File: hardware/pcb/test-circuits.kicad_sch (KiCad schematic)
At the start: 0 parts

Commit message: Update(hardware): Completed some schematics
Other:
- sheet Vibration LRA ports: added IN2, OUT+, OUT-; removed IN1
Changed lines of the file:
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@@
 		)
 		(pin "EN" input
+			(at 143.51 54.61 180)
+			(effects
+				(font
+					(size 1.27 1.27)
+				)
+				(justify left)
+			)
+		)
+		(pin "IN2" input
+			(at 143.51 60.96 180)
+			(effects
+				(font
+					(size 1.27 1.27)
+				)
+				(justify left)
+			)
+		)
+		(pin "OUT+" input
 			(at 165.1 54.61 0)
 			(effects
@@
 			)
 		)
-		(pin "IN1" input
+		(pin "OUT-" input
 			(at 165.1 60.96 0)
 			(effects

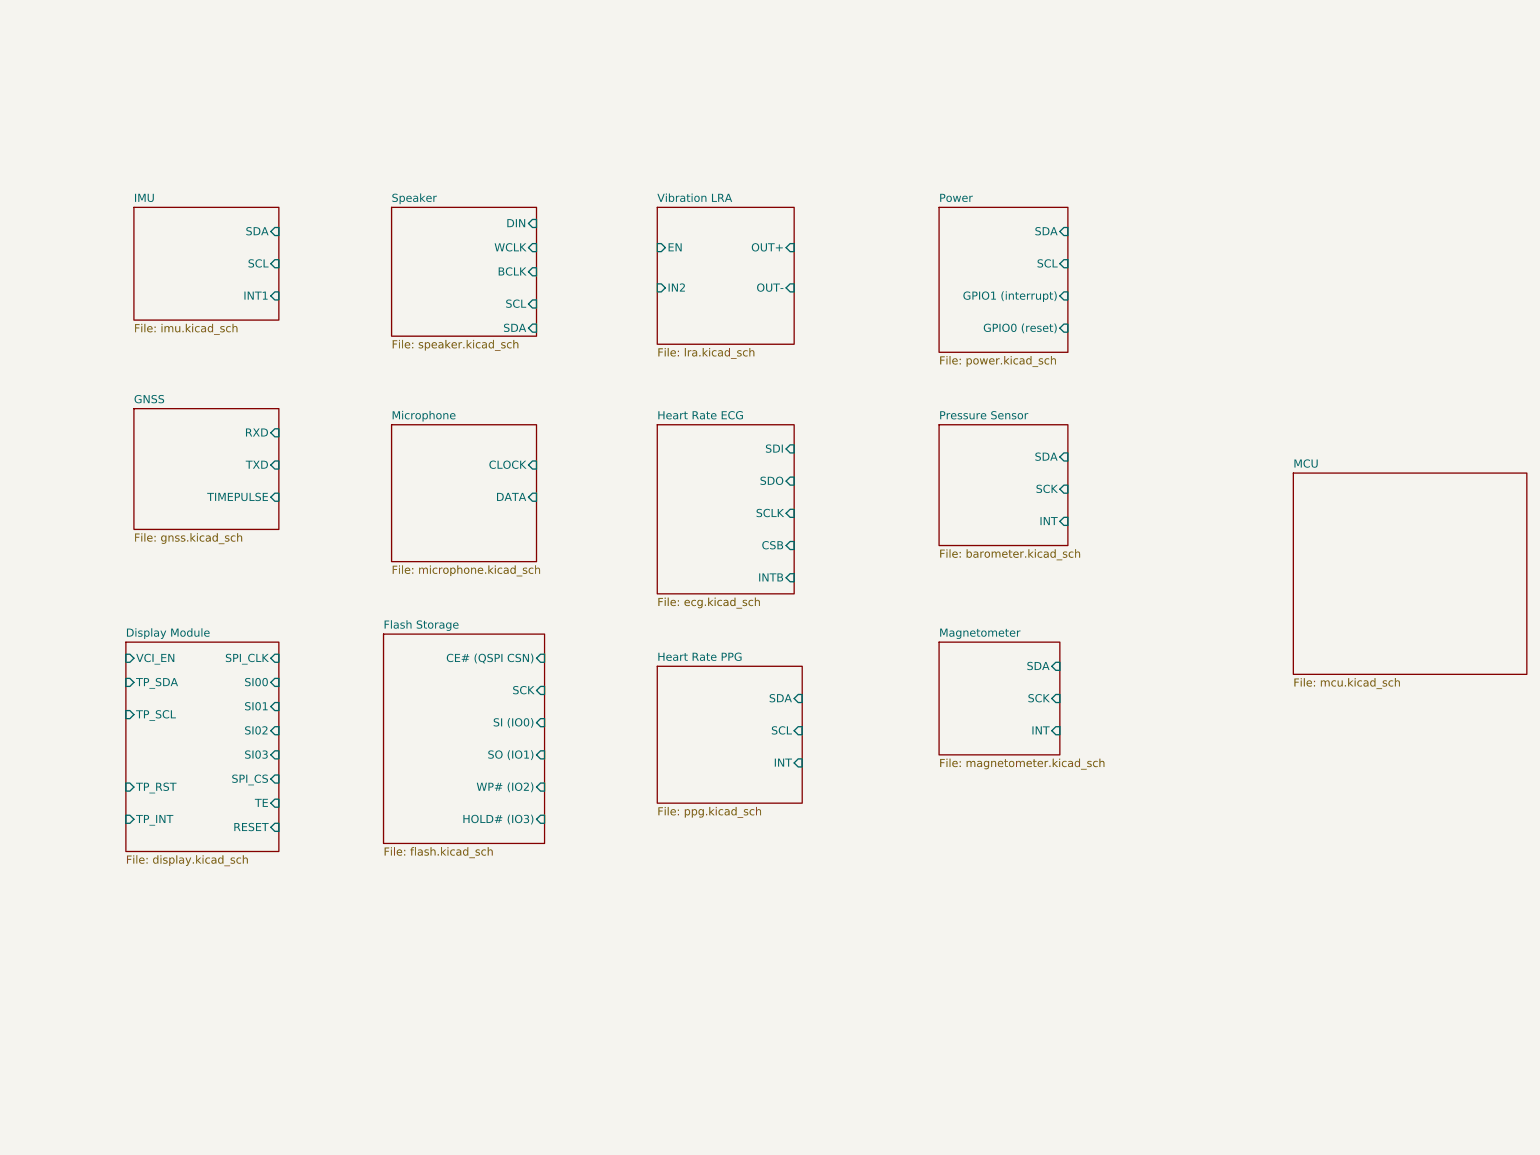
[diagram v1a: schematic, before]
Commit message: Changed GNDPWR to GND and changed GND to speciality GNDs
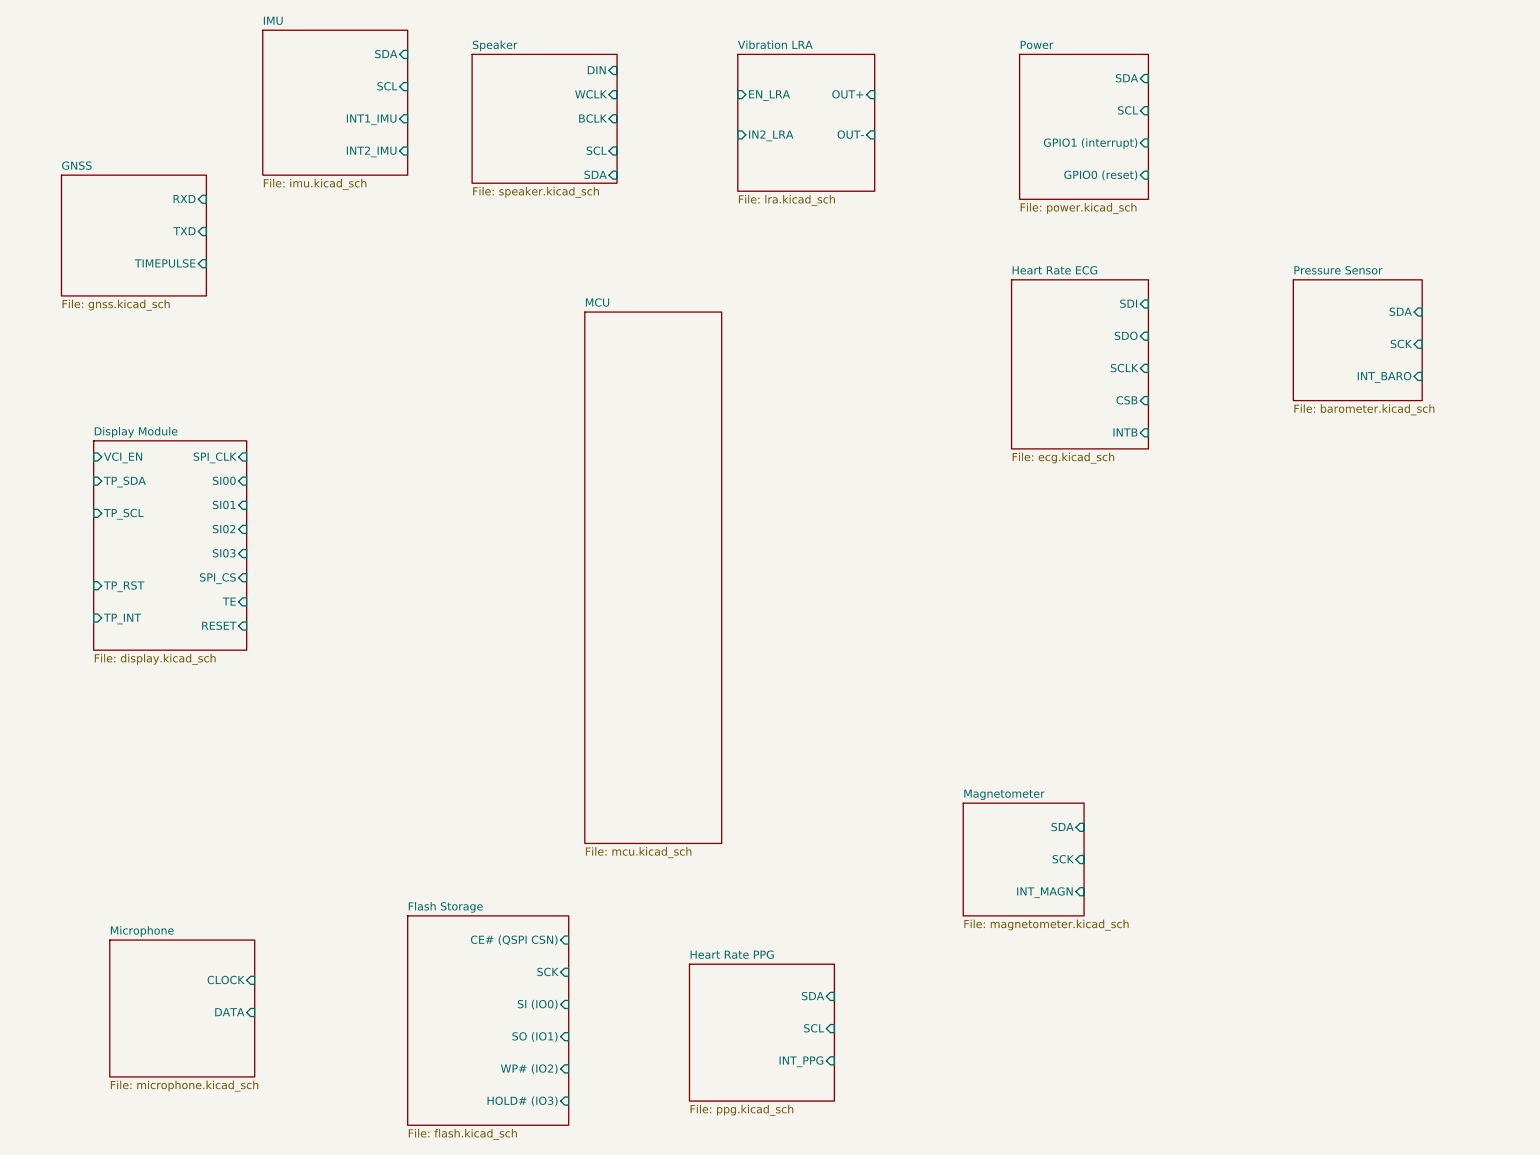
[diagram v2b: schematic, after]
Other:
- sheet Heart Rate PPG ports: added INT_PPG; removed INT
- sheet IMU ports: added INT1_IMU, INT2_IMU; removed INT1
- sheet Magnetometer ports: added INT_MAGN; removed INT
- sheet Pressure Sensor ports: added INT_BARO; removed INT
- sheet Vibration LRA ports: added EN_LRA, IN2_LRA; removed EN, IN2

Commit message: Added USB-C to UART connectivity for debugging and flashing
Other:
- added sheet Connector (connector.kicad_sch)
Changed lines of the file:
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@@
+	)
+	(sheet
+		(at 41.91 125.73)
+		(size 20.32 22.86)
+		(exclude_from_sim no)
+		(in_bom yes)
+		(on_board yes)
+		(dnp no)
+		(fields_autoplaced yes)
+		(stroke
+			(width 0.1524)
+			(type solid)
+		)
+		(fill
+			(color 0 0 0 0)
+		)
+		(property "Sheetname" "Connector"
+			(at 41.91 125.0184 0)
+			(show_name no)
+			(do_not_autoplace no)
+			(effects
+				(font
+					(size 1.27 1.27)
+				)
+				(justify left bottom)
+			)
+		)
+		(property "Sheetfile" "connector.kicad_sch"
+			(at 41.91 149.1746 0)
+			(show_name no)
+			(do_not_autoplace no)
+			(effects
+				(font
+					(size 1.27 1.27)
+				)
+				(justify left top)
+			)
+		)
+		(pin "DBG_UART_RXD" input
+			(at 62.23 129.54 0)
+			(effects
+				(font
+					(size 1.27 1.27)
+				)
+				(justify right)
+			)
+		)
+		(pin "DBG_UART_TXD" input
+			(at 62.23 134.62 0)
+			(effects
+				(font
+					(size 1.27 1.27)
+				)
+				(justify right)
+			)
+		)
+		(pin "SCL_USB" input
+			(at 62.23 139.7 0)
+			(effects
+				(font
+					(size 1.27 1.27)
+				)
+				(justify right)
+			)
+		)
+		(pin "SDA_USB" input
+			(at 62.23 144.78 0)
+			(effects
+				(font
+					(size 1.27 1.27)
+				)
+				(justify right)
+			)
+		)
+		(instances
+			(project "test-circuits"
+				(path "/7b1b7b91-6618-446c-b915-39ecd9748633"
+					(page "15")
+				)
+			)
+		)
 	)
 	(sheet

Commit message: Updated broken flash schematic.
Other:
- sheet Flash Storage ports: added FLASH CS#, FLASH IO0, FLASH IO1, FLASH IO2, FLASH IO3, FLASH SCK; removed CE# (QSPI CSN), HOLD# (IO3), SCK, SI (IO0), SO (IO1), WP# (IO2)
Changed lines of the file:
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@@
+	)
+	(sheet
+		(at 198.12 99.06)
+		(size 25.4 30.48)
+		(exclude_from_sim no)
+		(in_bom yes)
+		(on_board yes)
+		(dnp no)
+		(fields_autoplaced yes)
+		(stroke
+			(width 0.1524)
+			(type solid)
+		)
+		(fill
+			(color 0 0 0 0)
+		)
+		(property "Sheetname" "Flash Storage"
+			(at 198.12 98.3484 0)
+			(show_name no)
+			(do_not_autoplace no)
+			(effects
+				(font
+					(size 1.27 1.27)
+				)
+				(justify left bottom)
+			)
+		)
+		(property "Sheetfile" "flash.kicad_sch"
+			(at 198.12 130.1246 0)
+			(show_name no)
+			(do_not_autoplace no)
+			(effects
+				(font
+					(size 1.27 1.27)
+				)
+				(justify left top)
+			)
+		)
+		(pin "FLASH CS#" input
+			(at 198.12 104.14 180)
+			(effects
+				(font
+					(size 1.27 1.27)
+				)
+				(justify left)
+			)
+		)
+		(pin "FLASH IO0" input
+			(at 198.12 113.03 180)
+			(effects
+				(font
+					(size 1.27 1.27)
+				)
+				(justify left)
+			)
+		)
+		(pin "FLASH IO1" input
+			(at 198.12 116.84 180)
+			(effects
+				(font
+					(size 1.27 1.27)
+				)
+				(justify left)
+			)
+		)
+		(pin "FLASH IO2" input
+			(at 198.12 120.65 180)
+			(effects
+				(font
+					(size 1.27 1.27)
+				)
+				(justify left)
+			)
+		)
+		(pin "FLASH IO3" input
+			(at 198.12 124.46 180)
+			(effects
+				(font
+					(size 1.27 1.27)
+				)
+				(justify left)
+			)
+		)
+		(pin "FLASH SCK" input
+			(at 198.12 107.95 180)
+			(effects
+				(font
+					(size 1.27 1.27)
+				)
+				(justify left)
+			)
+		)
+		(instances
+			(project "test-circuits"
+				(path "/7b1b7b91-6618-446c-b915-39ecd9748633"
+					(page "13")
+				)
+			)
+		)
 	)
 	(sheet
@@
 				)
 			)
-		)
-	)
-	(sheet
-		(at 104.14 160.02)
-		(size 25.4 33.02)
-		(exclude_from_sim no)
-		(in_bom yes)
-		(on_board yes)
-		(dnp no)
-		(fields_autoplaced yes)
-		(stroke
-			(width 0.1524)
-			(type solid)
-		)
-		(fill
-			(color 0 0 0 0)
-		)
-		(property "Sheetname" "Flash Storage"
-			(at 104.14 159.3084 0)
-			(show_name no)
-			(do_not_autoplace no)
-			(effects
-				(font
-					(size 1.27 1.27)
-				)
-				(justify left bottom)
-			)
-		)
-		(property "Sheetfile" "flash.kicad_sch"
-			(at 104.14 193.6246 0)
-			(show_name no)
-			(do_not_autoplace no)
-			(effects
-				(font
-					(size 1.27 1.27)
-				)
-				(justify left top)
-			)
-		)
-		(pin "CE# (QSPI CSN)" input
-			(at 129.54 163.83 0)
-			(effects
-				(font
-					(size 1.27 1.27)
-				)
-				(justify right)
-			)
-		)
-		(pin "HOLD# (IO3)" input
-			(at 129.54 189.23 0)
-			(effects
-				(font
-					(size 1.27 1.27)
-				)
-				(justify right)
-			)
-		)
-		(pin "SCK" input
-			(at 129.54 168.91 0)
-			(effects
-				(font
-					(size 1.27 1.27)
-				)
-				(justify right)
-			)
-		)
-		(pin "SI (IO0)" input
-			(at 129.54 173.99 0)
-			(effects
-				(font
-					(size 1.27 1.27)
-				)
-				(justify right)
-			)
-		)
-		(pin "SO (IO1)" input
-			(at 129.54 179.07 0)
-			(effects
-				(font
-					(size 1.27 1.27)
-				)
-				(justify right)
-			)
-		)
-		(pin "WP# (IO2)" input
-			(at 129.54 184.15 0)
-			(effects
-				(font
-					(size 1.27 1.27)
-				)
-				(justify right)
-			)
-		)
-		(instances
-			(project "test-circuits"
-				(path "/7b1b7b91-6618-446c-b915-39ecd9748633"
-					(page "13")
-				)
-			)
